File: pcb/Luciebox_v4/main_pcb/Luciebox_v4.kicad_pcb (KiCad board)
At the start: 2 copper layers, 78 x 92 mm, 64 parts, among them J1 USB_B_Mini, J2 USB_B_Mini, Q1 P-Channel MOSFET, Q2 NPN transistor, T1 terminal_8x1, T2 terminal_3x1, T4 terminal_8x1, T5 terminal_3x1, T6 terminal_8x1, T7 terminal_8x1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

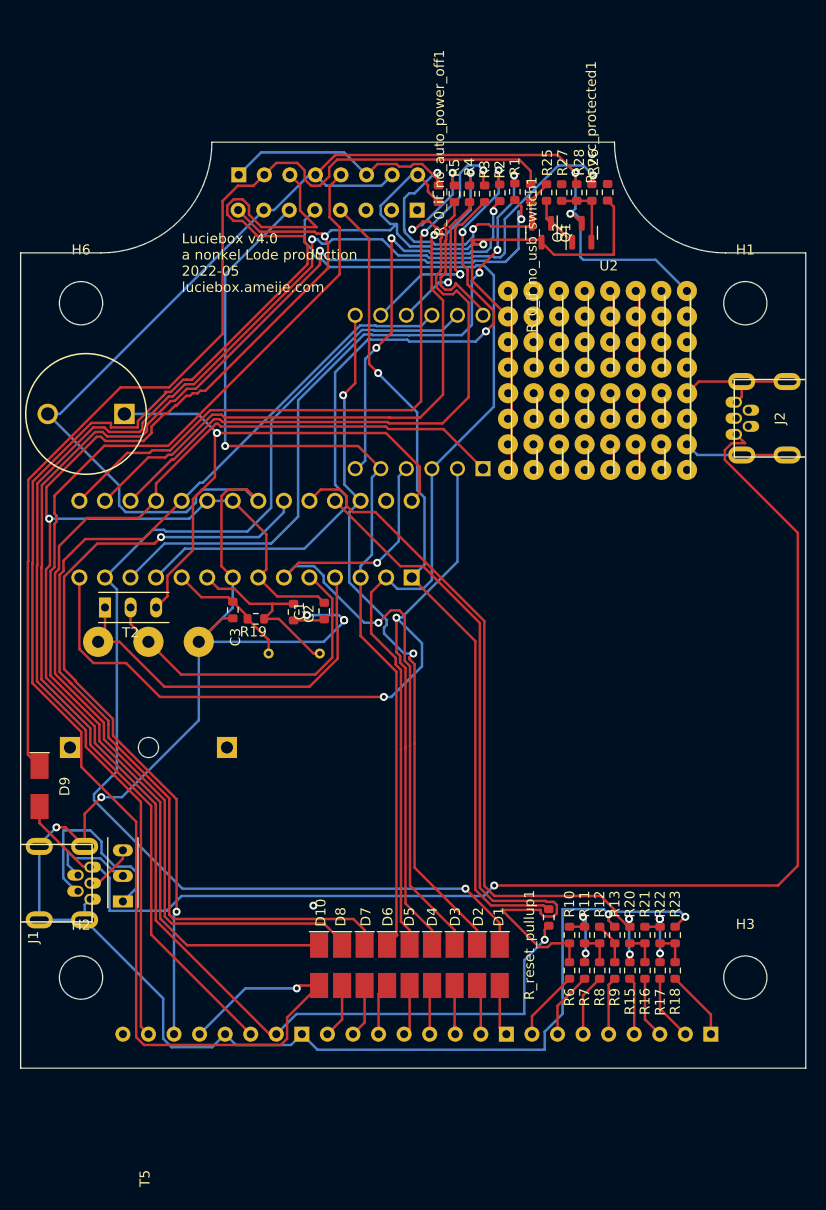
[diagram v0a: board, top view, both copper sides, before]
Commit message: Add artwork. Copy screenshot to gimp to delete parts you don't want with silkscreen from original image. Than, generate new artwork. from burst, set to 150mm export
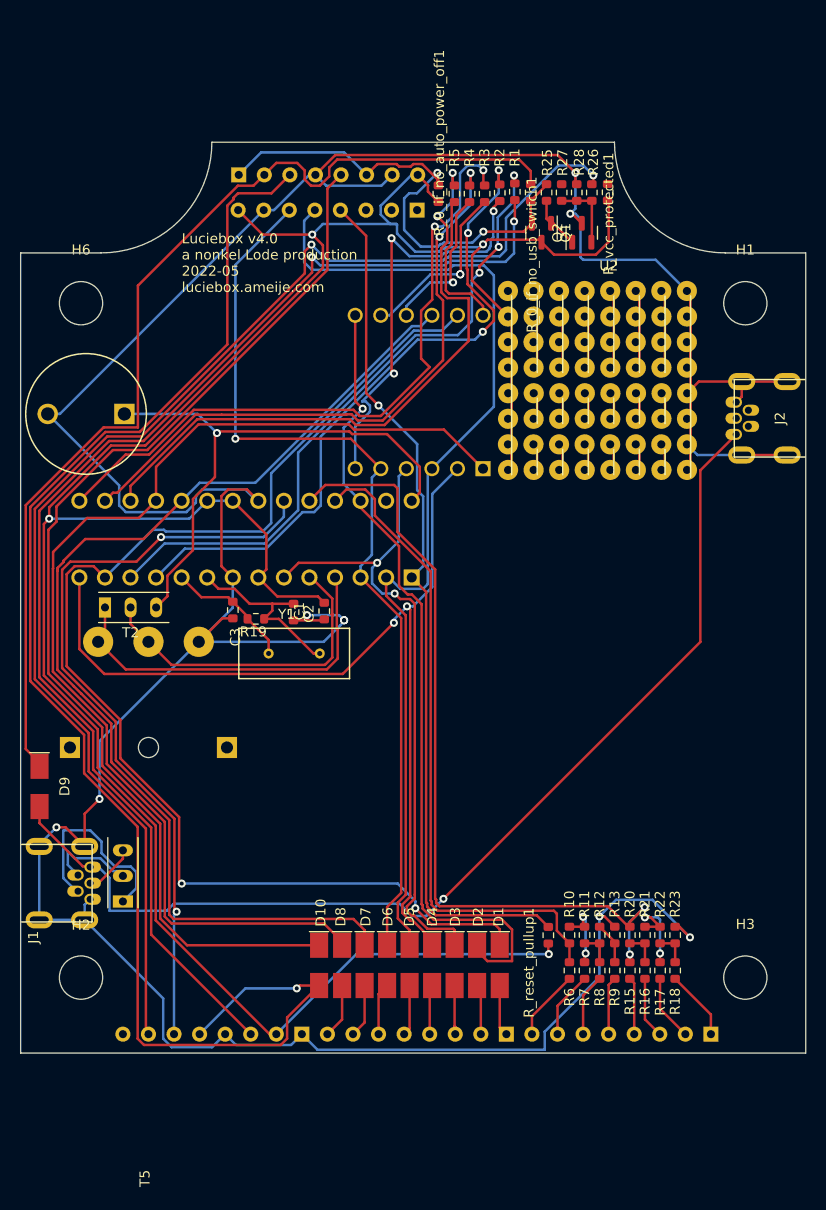
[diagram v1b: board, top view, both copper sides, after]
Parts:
- added G***: LOGO, artworkv4:burst_luciebox_v4 150, B.Cu at (38.5, 21.5)
- Y1: moved to F.Cu
- moved R_reset_pullup1 1.77 mm to (52.4, 78.8)
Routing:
- net Net-(D9-Pad2): track 132.2 -> 107.0 mm
- net Net-(D10-Pad2): track 162.4 -> 140.7 mm
- net /A3: track 70.6 -> 80.9 mm, vias 2 -> 1
- net /A1: track 71.7 -> 81.3 mm
- net VCC: track 261.8 -> 252.2 mm
- net /11(PWM-MOSI): track 70.2 -> 63.2 mm
- net /8: track 101.9 -> 95.3 mm
- net /5(PWM): track 73.1 -> 67.0 mm
- net /A2: track 71.3 -> 65.6 mm
- net /4: track 71.1 -> 65.6 mm
- net Net-(R_reset_pullup1-Pad2): track 82.1 -> 86.6 mm
- net Net-(R1-Pad1): track 129.6 -> 125.4 mm
- net /6(PWM): track 68.6 -> 64.9 mm
- net Net-(R26-Pad2): track 135.3 -> 132.3 mm
- net /10(PWM-SS): track 64.3 -> 61.4 mm
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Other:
- board size 78 x 92 mm -> 78 x 90.5 mm
- board text added: "B1"
- board text added: "B1 B1 + B5 B1 + B8 B1 + B6"
- board text added: "B1 B2,B3 B4 B5,B6,B7,B8"
- board text added: "B2"
- board text added: "B3"
- board text added: "B4"
- board text added: "B5"
- board text added: "B6"
- board text added: "B7"
- board text added: "B8"
- board text added: "Buttons Control Button Options|Shift Start|Stop|Auto Action Buttons"
- board text added: "Control Box On Box Off App Select App Reset"
- board text added: "Luciebox Apps 1 Settings 2 Stopwatch 3 MultiTimer 4 School 5 Pomodoro 6 Random 7 Score 8 Simon 9 Reaction 10 Wackamole 11 Guitar Hero"
- board text added: "luciebox"
- board text removed: "Applications 1 Settings 2 Stopwatch 3 MultiTimer 4 School 5 Pomodoro 6 Random 7 Score 8 Simon 9 Reaction 10 Wackamole 11 Guitar Hero"
- board text removed: "ON: B1 OFF: B1 + B5 APP SELECT: B1 + B8 APP RESET: B1 + B6"

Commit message: Add extra text and adjust artwork
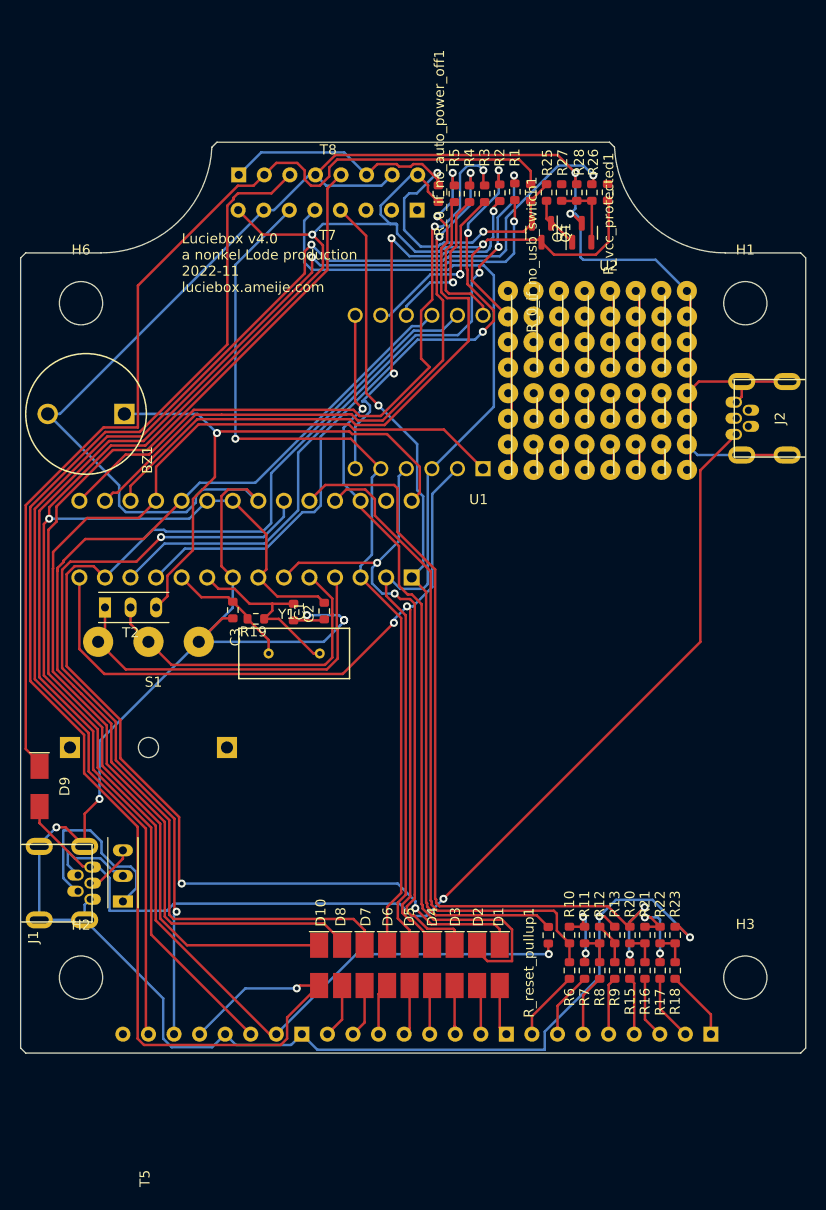
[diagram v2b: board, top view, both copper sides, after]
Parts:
- removed the G*** at (38.5, 21.5)
- added G***: LOGO, artworkv4:burst_luciebox_v4 b150, B.Cu at (38.6, 21.3)
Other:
- outline, holes or cut-outs redrawn
- board text added: "A Nonkel Lode Production | 2022"
- board text added: "Detailed Instruction Manual at ameije.com"
- board text added: "Luciebox v4.0 a nonkel Lode production 2022-11 luciebox.ameije.com"
- board text removed: "Luciebox v4.0 a nonkel Lode production 2022-05 luciebox.ameije.com"

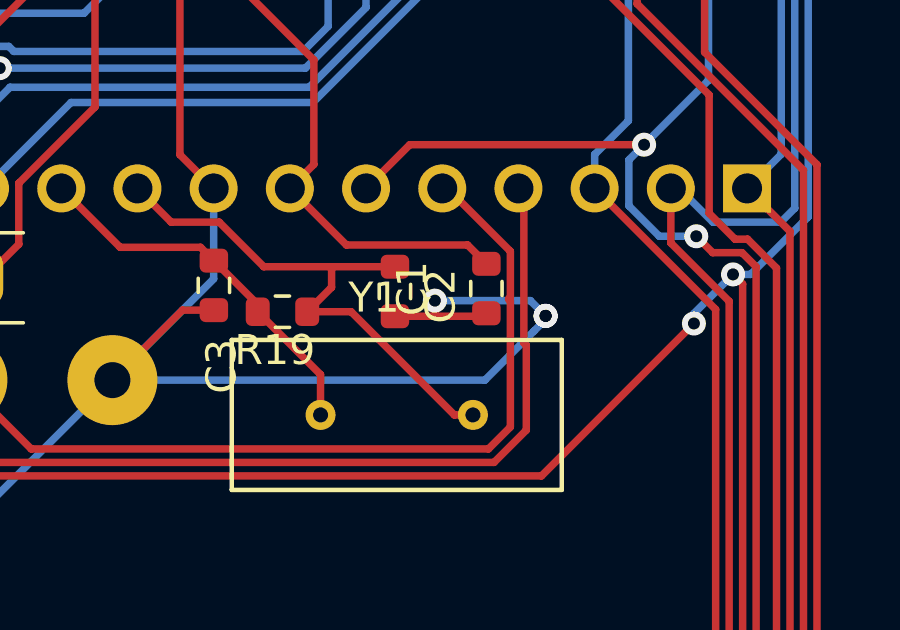
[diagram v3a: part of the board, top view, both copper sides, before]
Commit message: Main pcb v4 values
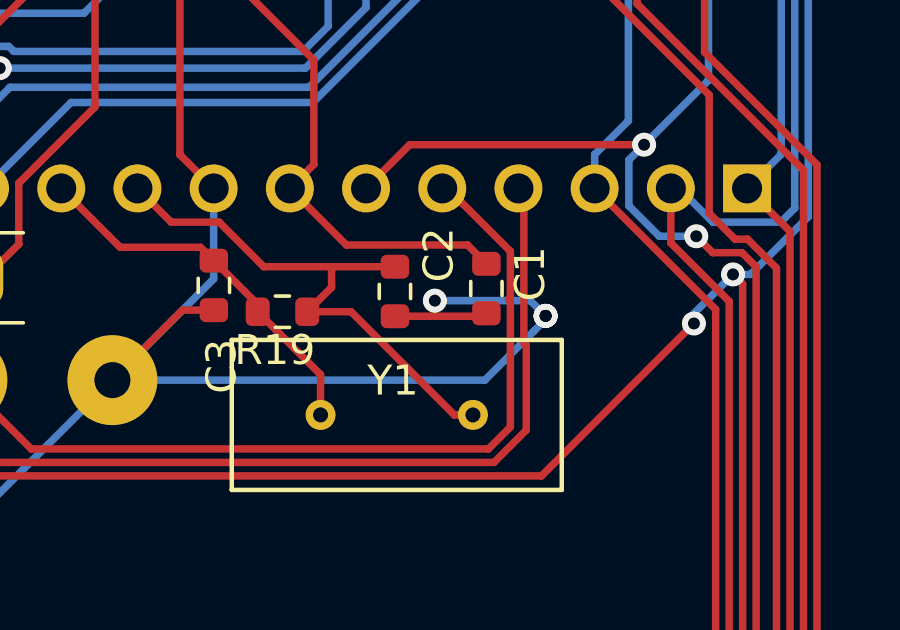
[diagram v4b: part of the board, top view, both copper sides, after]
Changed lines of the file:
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@@
     (property "Sheetname" "")
     (attr smd)
-    (fp_text reference "C2" (at -0.157 1.524 90) (layer "F.SilkS")
+    (fp_text reference "C2" (at 1.219 1.457 90) (layer "F.SilkS")
       (effects (font (size 1 1) (thickness 0.15)))
     )
@@
     (property "Sheetname" "")
     (attr through_hole)
-    (fp_text reference "Y1" (at 0.76 3.91) (layer "F.SilkS")
+    (fp_text reference "Y1" (at 0.127 1.143) (layer "F.SilkS")
       (effects (font (size 1 1) (thickness 0.15)))
     )
@@
     (property "Sheetname" "")
     (attr smd)
-    (fp_text reference "C1" (at 0 2.472 90) (layer "F.SilkS")
-      (effects (font (size 1 1) (thickness 0.15)))
-    )
+    (fp_text reference "C1" (at -0.487 -1.457 90) (layer "F.SilkS")
+      (effects (font (size 1 1) (thickness 0.15)))
+    )
